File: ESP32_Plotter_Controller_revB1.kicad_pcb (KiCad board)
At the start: 2 copper layers, 99.1 x 55.4 mm, 61 parts, among them J1 ARM JTAG 10pin, J10 Pen Lift, J11 Vselect, J12 X Motor, J13 Y Motor, J14 Neo Pixel LEDs, J15 Pen Direction, J16 Aux Port (I2C), J17 USB_C_Receptacle_USB2.0, J18 E-Stop, J19 Y Limit Switch, J2 Power (12v), J3 5V Aux, J4 Vin Aux, J5 X Limit Switch, J6 Aux Port (SPI), J7 X Limit, J8 Micro_SD_Card_TF-01A, J9 Y Limit, SW1 RESET, SW2 BOOT, U1 ESP32-WROOM-32D, U2 TMC2130, U3 TMC2130, U4 XL1509, U5 CH340C, U6 AMS1117-3.3

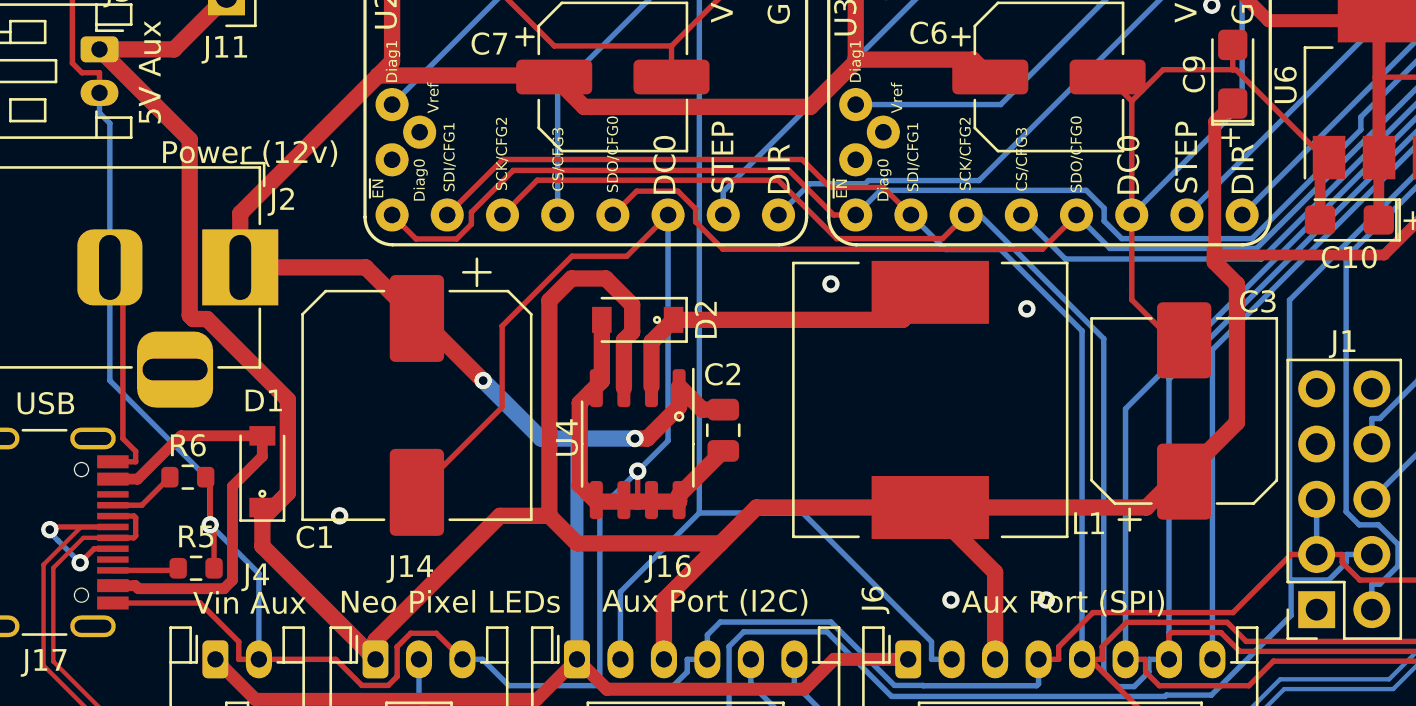
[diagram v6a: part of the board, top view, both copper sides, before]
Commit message: Change C3 COUT to 220uF
220uF is more readily available from LCSC and can use a better quality capacitor
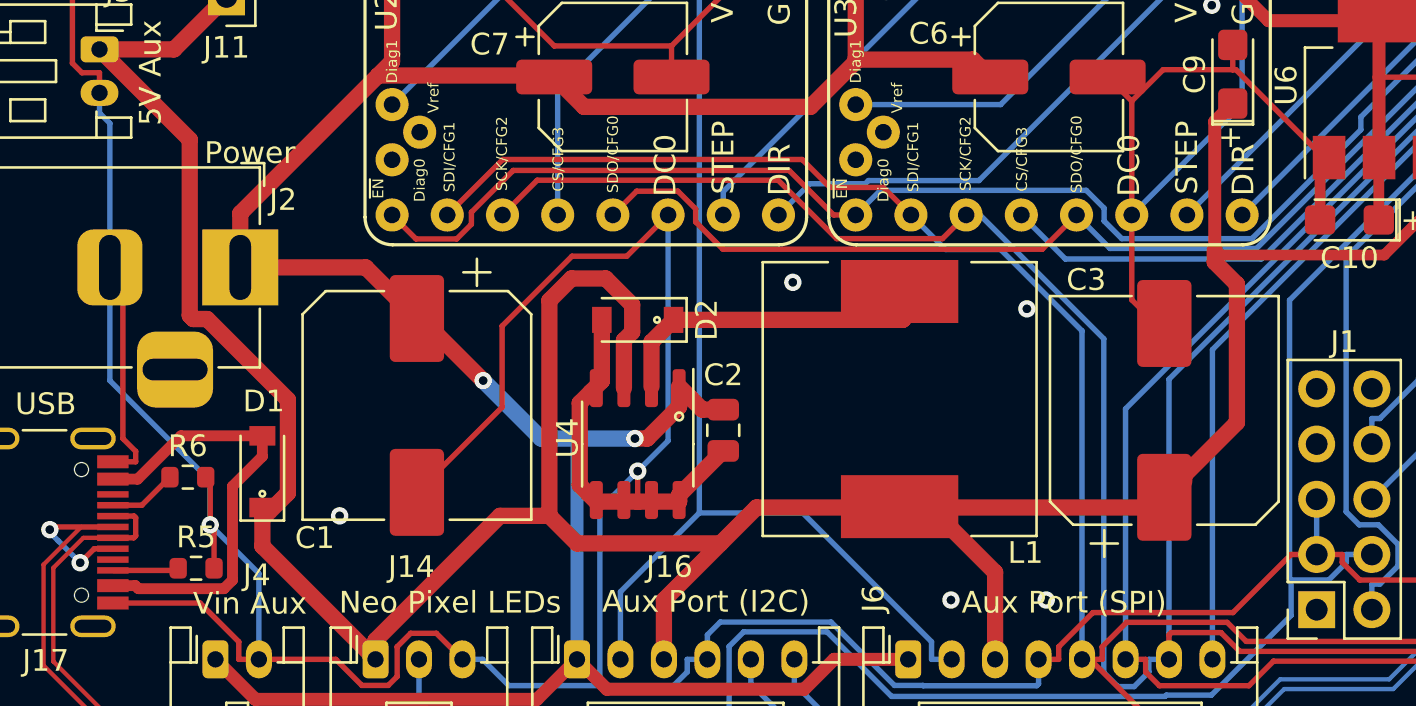
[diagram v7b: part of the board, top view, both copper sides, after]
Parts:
- C3: value 180uF 35v -> 220uF 50v; footprint Capacitor_SMD:CP_Elec_8x10 -> Capacitor_SMD:CP_Elec_10x10
- J2: value Power (12v) -> Power
- moved L1 1.41 mm to (69.7, 104.9)
- moved C3 0.91 mm to (81.9, 105.4)
